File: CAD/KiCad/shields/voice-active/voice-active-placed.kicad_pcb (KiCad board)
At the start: 2 copper layers, 30 x 42 mm, 30 parts, among them U1 MCP6024-I/SL

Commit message: Route the shield set and validate shared interfaces
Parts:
- moved CID1 3.04 mm to (77.0, 71.5)
- moved R8 2.50 mm to (77.0, 78.5)
- moved R7 2.00 mm to (77.0, 75.0)

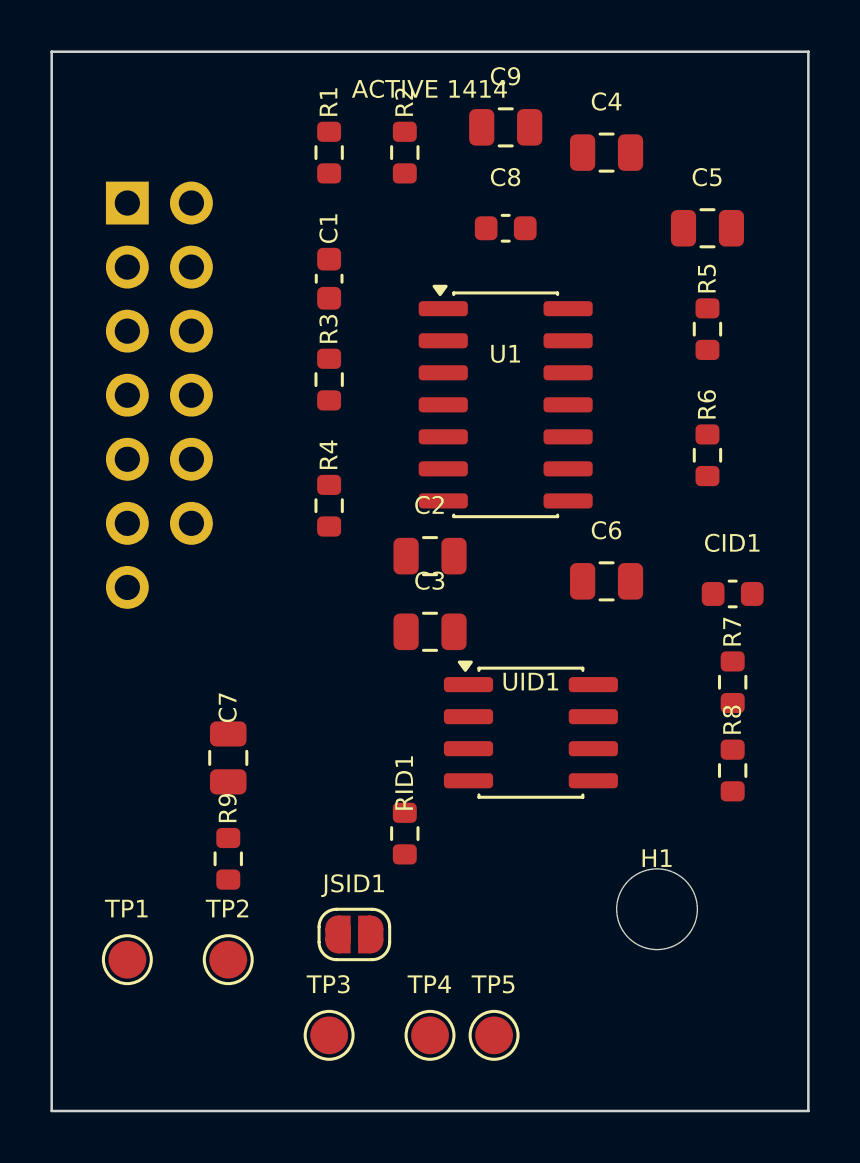
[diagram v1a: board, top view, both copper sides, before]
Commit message: Remove shield identification and adopt the simplified connector and Teensy pin maps
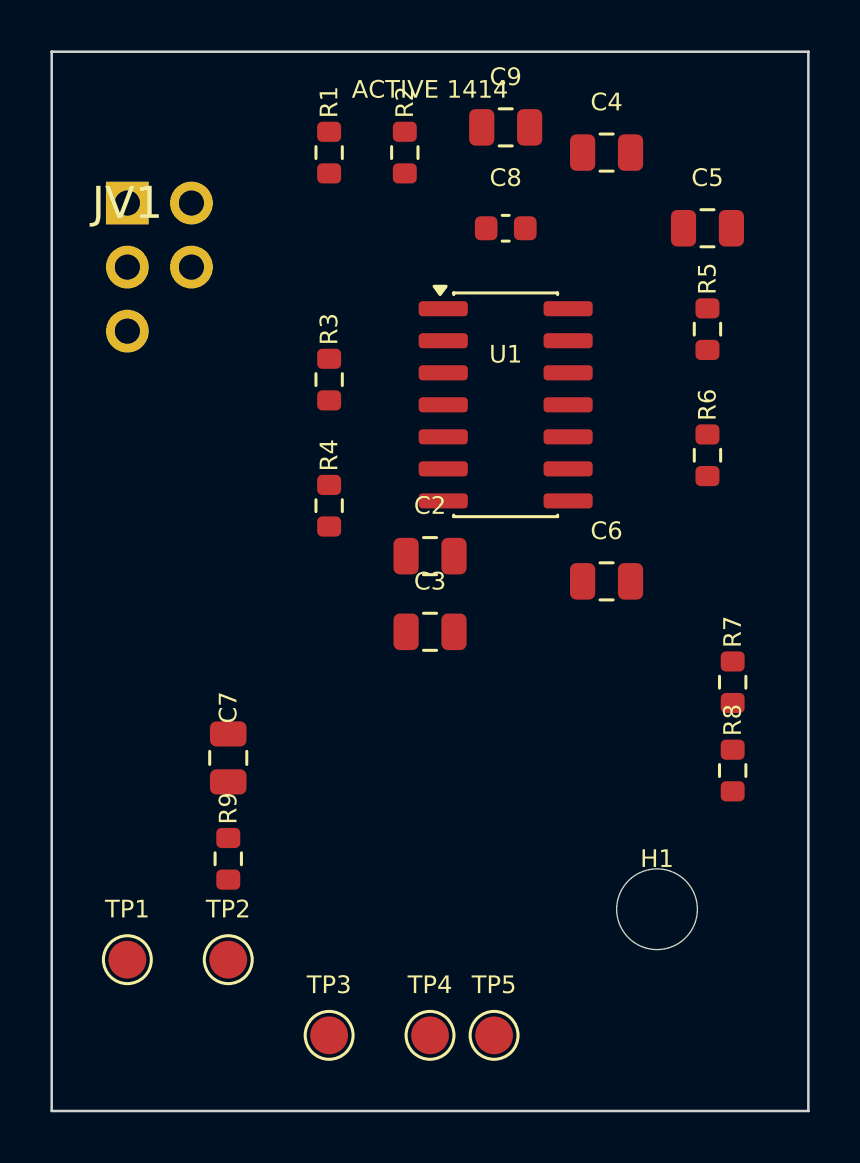
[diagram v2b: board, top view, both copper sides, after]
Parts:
- removed C1: 470pF C0G, Shields:C_0603_1608Metric
- removed CID1: 100nF, Shields:C_0603_1608Metric
- removed JSID1: WRITE ENABLE - OPEN, Shields:SolderJumper-2_P1.3mm_Open_RoundedPad1.0x1.5mm
- removed RID1: 10K, Shields:R_0603_1608Metric
- removed UID1: M24C02-RMN6TP, Shields:SOIC-8_3.9x4.9mm_P1.27mm
- JV1: value VOICE - KEY 14 -> VOICE - KEY 6; footprint Shields:Socket_2x07_Key14 -> Shields:Socket_2x03_Key6
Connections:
- JV1 pad 2: GND -> (no net)

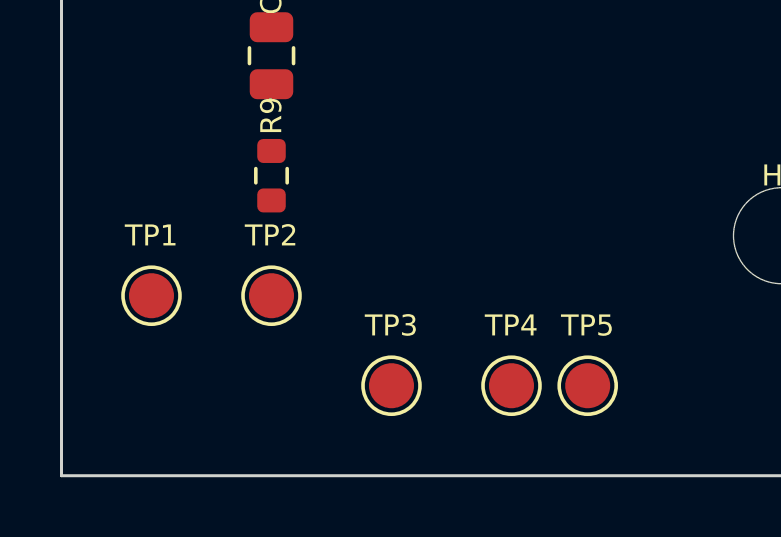
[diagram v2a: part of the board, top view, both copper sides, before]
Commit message: Finish revised shield routing, printed identification and clean KiCad checks
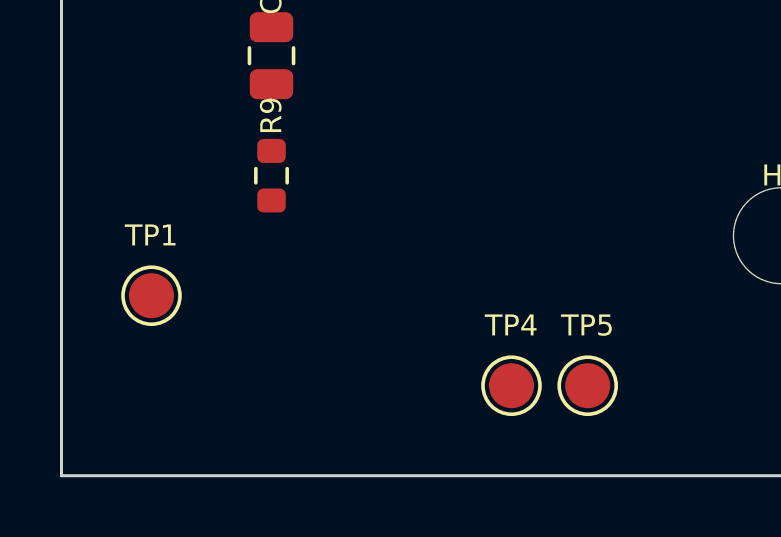
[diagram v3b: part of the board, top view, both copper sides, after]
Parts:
- removed TP2: input, Shields:TestPoint_Pad_D1.5mm
- removed TP3: stage1/out, Shields:TestPoint_Pad_D1.5mm
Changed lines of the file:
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@@
 		)
-	)
-	(footprint "Shields:TestPoint_Pad_D1.5mm"
-		(layer "F.Cu")
-		(at 61 89)
-		(descr "SMD pad as test Point, diameter 1.5mm")
-		(tags "test point SMD pad")
-		(property "Reference" "TP3"
-			(at 0 -2 0)
-			(layer "F.SilkS")
-			(effects
-				(font
-					(size 0.7 0.7)
-					(thickness 0.1)
-				)
-			)
-		)
-		(property "Value" "stage1/out"
-			(at 0 1.75 0)
-			(layer "F.Fab")
-			(hide yes)
-			(effects
-				(font
-					(size 1 1)
-					(thickness 0.15)
-				)
-			)
-		)
-		(property "Datasheet" ""
-			(at 0 0 0)
-			(unlocked yes)
-			(layer "F.Fab")
-			(hide yes)
-			(effects
-				(font
-					(size 1.27 1.27)
-					(thickness 0.15)
-				)
-			)
-		)
-		(property "Description" ""
-			(at 0 0 0)
-			(unlocked yes)
-			(layer "F.Fab")
-			(hide yes)
-			(effects
-				(font
-					(size 1.27 1.27)
-					(thickness 0.15)
-				)
-			)
-		)
-		(attr exclude_from_pos_files exclude_from_bom)
-		(fp_circle
-			(center 0 0)
-			(end 0 0.95)
-			(stroke
-				(width 0.12)
-				(type solid)
-			)
-			(fill no)
-			(layer "F.SilkS")
-		)
-		(fp_circle
-			(center 0 0)
-			(end 1.25 0)
-			(stroke
-				(width 0.05)
-				(type solid)
-			)
-			(fill no)
-			(layer "F.CrtYd")
-		)
-		(fp_text user "${REFERENCE}"
-			(at 0 -1.65 0)
-			(layer "F.Fab")
-			(effects
-				(font
-					(size 1 1)
-					(thickness 0.15)
-				)
-			)
-		)
-		(pad "1" smd circle
-			(at 0 0)
-			(size 1.5 1.5)
-			(layers "F.Cu" "F.Mask")
-			(net 9 "stage1{slash}out")
-		)
-		(embedded_fonts no)
 	)
 	(footprint "Shields:C_0805_2012Metric"
@@
 			)
 		)
-	)
-	(footprint "Shields:TestPoint_Pad_D1.5mm"
-		(layer "F.Cu")
-		(at 57 86)
-		(descr "SMD pad as test Point, diameter 1.5mm")
-		(tags "test point SMD pad")
-		(property "Reference" "TP2"
-			(at 0 -2 0)
-			(layer "F.SilkS")
-			(effects
-				(font
-					(size 0.7 0.7)
-					(thickness 0.1)
-				)
-			)
-		)
-		(property "Value" "input"
-			(at 0 1.75 0)
-			(layer "F.Fab")
-			(hide yes)
-			(effects
-				(font
-					(size 1 1)
-					(thickness 0.15)
-				)
-			)
-		)
-		(property "Datasheet" ""
-			(at 0 0 0)
-			(unlocked yes)
-			(layer "F.Fab")
-			(hide yes)
-			(effects
-				(font
-					(size 1.27 1.27)
-					(thickness 0.15)
-				)
-			)
-		)
-		(property "Description" ""
-			(at 0 0 0)
-			(unlocked yes)
-			(layer "F.Fab")
-			(hide yes)
-			(effects
-				(font
-					(size 1.27 1.27)
-					(thickness 0.15)
-				)
-			)
-		)
-		(attr exclude_from_pos_files exclude_from_bom)
-		(fp_circle
-			(center 0 0)
-			(end 0 0.95)
-			(stroke
-				(width 0.12)
-				(type solid)
-			)
-			(fill no)
-			(layer "F.SilkS")
-		)
-		(fp_circle
-			(center 0 0)
-			(end 1.25 0)
-			(stroke
-				(width 0.05)
-				(type solid)
-			)
-			(fill no)
-			(layer "F.CrtYd")
-		)
-		(fp_text user "${REFERENCE}"
-			(at 0 -1.65 0)
-			(layer "F.Fab")
-			(effects
-				(font
-					(size 1 1)
-					(thickness 0.15)
-				)
-			)
-		)
-		(pad "1" smd circle
-			(at 0 0)
-			(size 1.5 1.5)
-			(layers "F.Cu" "F.Mask")
-			(net 5 "input")
-		)
-		(embedded_fonts no)
 	)
 	(footprint "Shields:MountingHole_3.2mm_M3"
@@
 			(size 1.7 1.7)
 			(drill 1)
-			(layers "*.Cu")
+			(layers "*.Cu" "*.Mask")
 			(remove_unused_layers no)
 			(net 13 "tone")
@@
 			(size 1.7 1.7)
 			(drill 1)
-			(layers "*.Cu")
+			(layers "*.Cu" "*.Mask")
 			(remove_unused_layers no)
 			(thermal_bridge_angle 45)
@@
 			(size 1.7 1.7)
 			(drill 1)
-			(layers "*.Cu")
+			(layers "*.Cu" "*.Mask")
 			(remove_unused_layers no)
 			(net 4 "filter out")
@@
 			(size 1.7 1.7)
 			(drill 1)
-			(layers "*.Cu")
+			(layers "*.Cu" "*.Mask")
 			(remove_unused_layers no)
 			(net 2 "AGND")
@@
 			(size 1.7 1.7)
 			(drill 1)
-			(layers "*.Cu")
+			(layers "*.Cu" "*.Mask")
 			(remove_unused_layers no)
 			(net 1 "+5V")

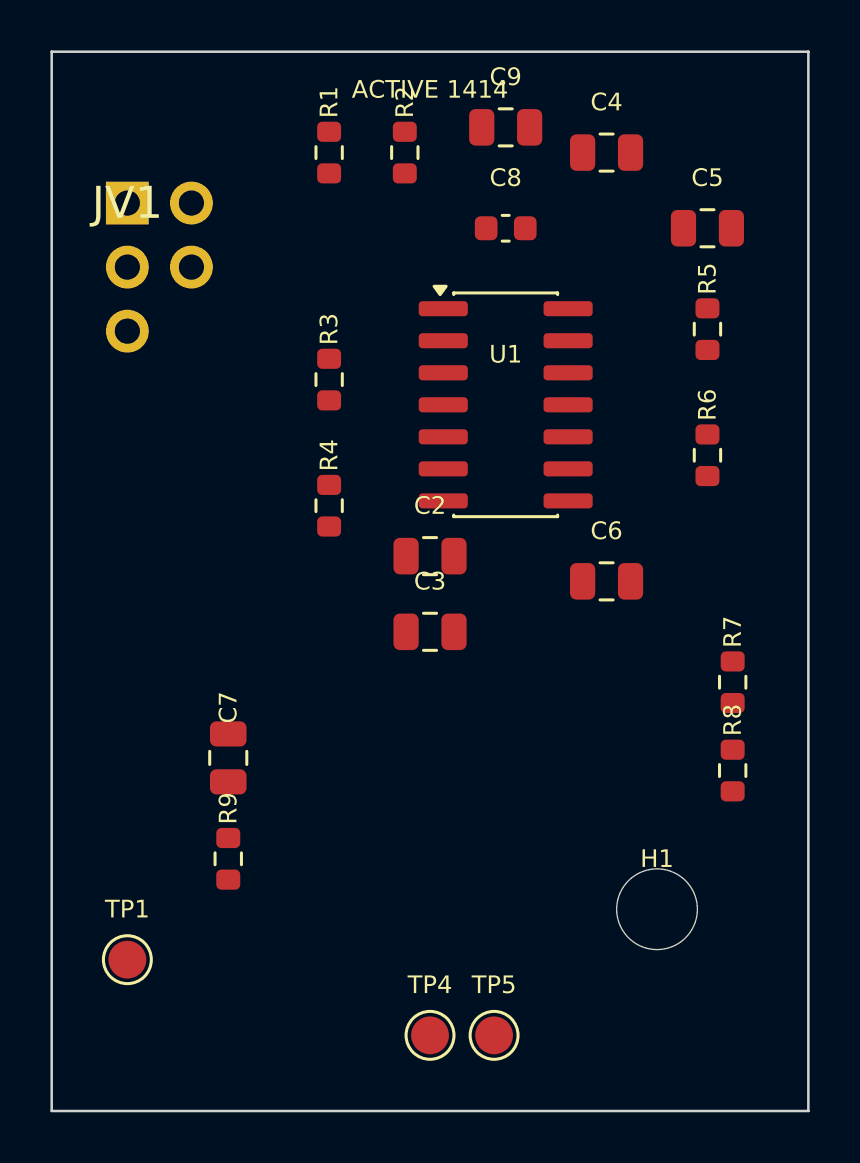
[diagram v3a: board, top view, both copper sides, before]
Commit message: Route microphones directly to Teensy and remove the analyser buffer board
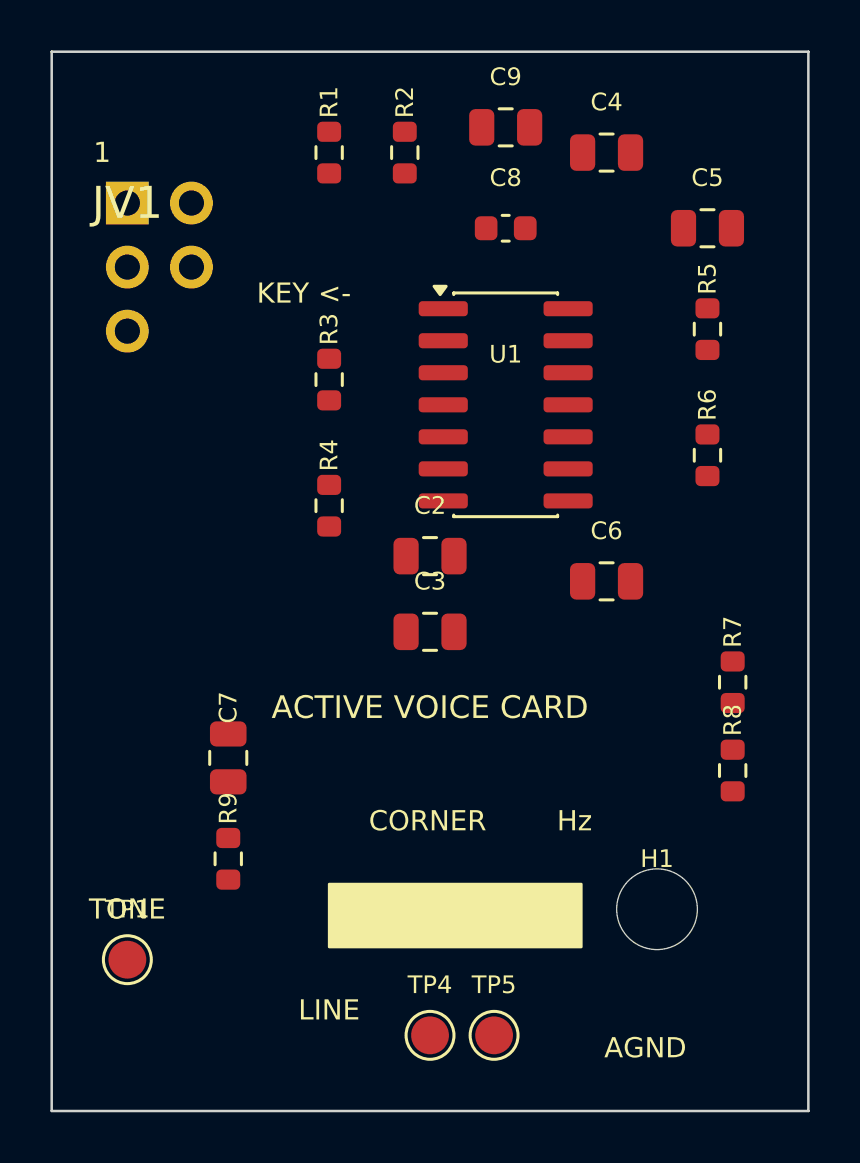
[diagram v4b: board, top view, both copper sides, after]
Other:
- board text added: "1"
- board text added: "1.27K"
- board text added: "1.65K"
- board text added: "1.82K"
- board text added: "10.2K"
- board text added: "1000"
- board text added: "105K"
- board text added: "11314"
- board text added: "13.3K"
- board text added: "14.7K"
- board text added: "1414"
- board text added: "177"
- board text added: "18.7K"
- board text added: "2.32K"
- board text added: "2.55K"
- board text added: "20.5K"
- board text added: "2000"
- board text added: "250"
- board text added: "26.7K"
- board text added: "2828"
- board text added: "29.4K"
- board text added: "3.32K"
- board text added: "3.65K"
- board text added: "354"
- board text added: "37.4K"
- board text added: "4.64K"
- board text added: "4000"
- board text added: "41.2K"
- board text added: "5.11K"
- board text added: "500"
- board text added: "52.3K"
- board text added: "5657"
- board text added: "57.6K"
- board text added: "6.65K"
- board text added: "7.32K"
- board text added: "707"
- board text added: "75K"
- board text added: "8000"
- board text added: "82.5K"
- board text added: "9.31K"
- board text added: "ACTIVE VOICE CARD"
- board text added: "AGND"
- board text added: "CORNER"
- board text added: "CORNER Hz"
- board text added: "FIT"
- board text added: "KEY <-"
- board text added: "LINE"
- board text added: "PLAY 0.5-1 x CORNER BEST 0.6-0.85 x CORNER"
- board text added: "Ra"
- board text added: "Rb"
- board text added: "TONE"
- board text removed: "ACTIVE 1414"
- board text removed: "ALLOW 707-1414 / IDLE 1MHz"
- board text removed: "SWEET 849-1202"
